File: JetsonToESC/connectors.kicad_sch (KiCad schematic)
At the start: 13 parts, among them J1 Conn_01x12, J2 Conn_01x03, J3 Conn_01x02, J4 Screw_Terminal_01x01, J5 Screw_Terminal_01x01

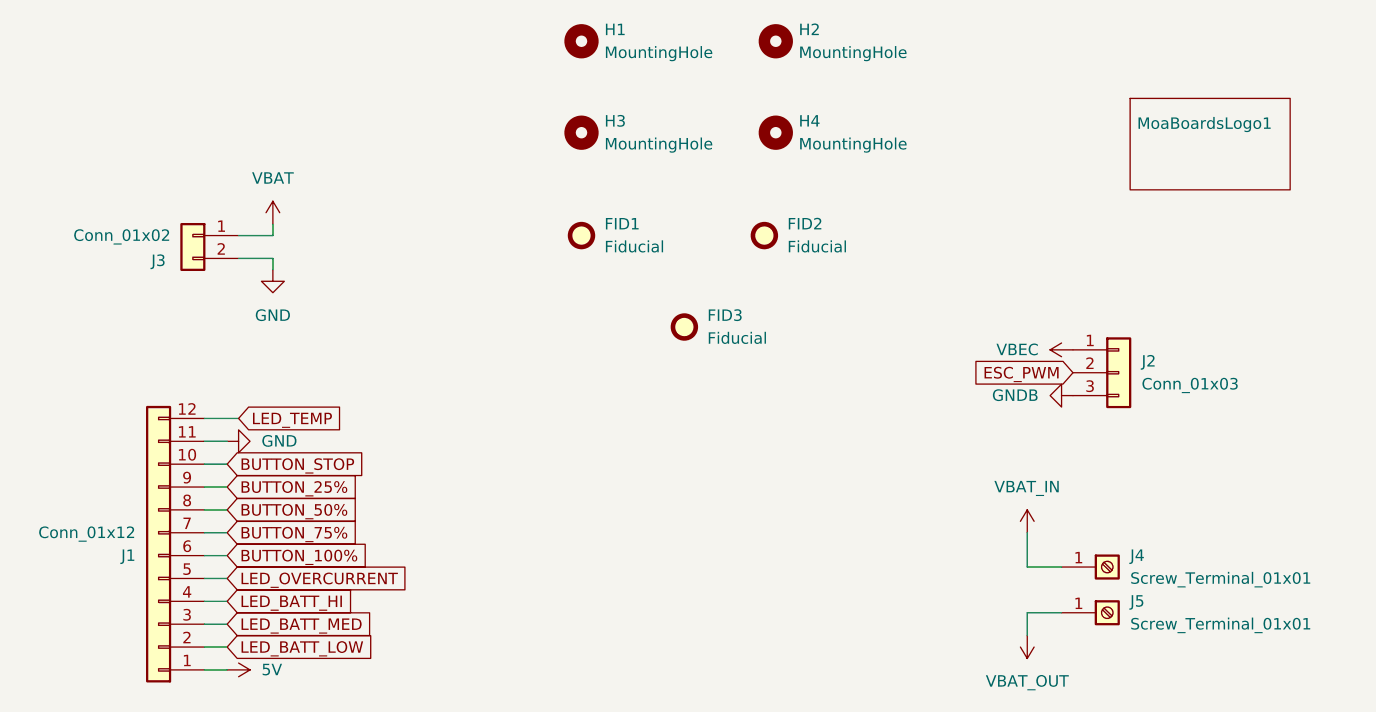
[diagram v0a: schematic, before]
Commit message: Added UART header
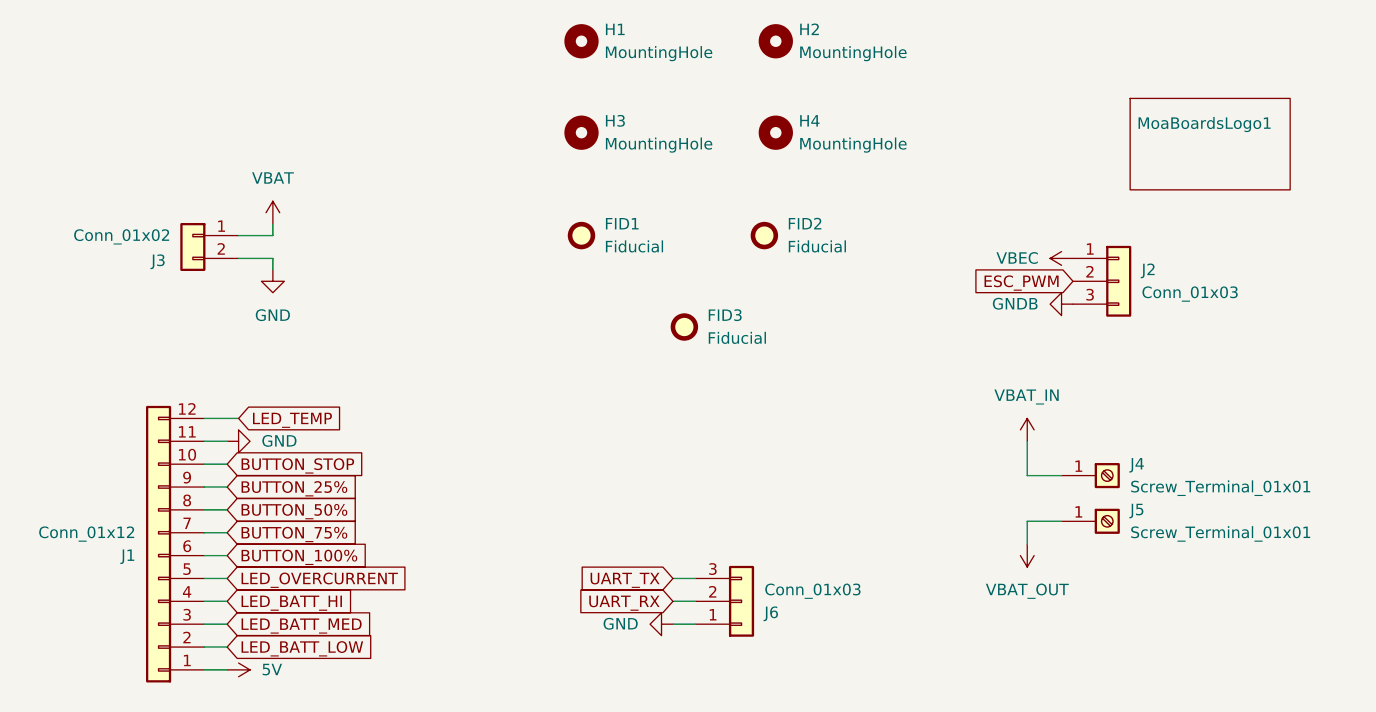
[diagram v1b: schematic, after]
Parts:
- added J6: Conn_01x03, Connector_PinHeader_2.54mm:PinHeader_1x03_P2.54mm_Vertical, symbol Connector_Generic:Conn_01x03
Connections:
- net GND: now also J6.1 (Pin_1)
- new net UART_RX: J6.2 (Pin_2)
- new net UART_TX: J6.3 (Pin_3)
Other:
- moved on the sheet: J2, J4, J5
